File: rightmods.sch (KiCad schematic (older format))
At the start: 28 parts

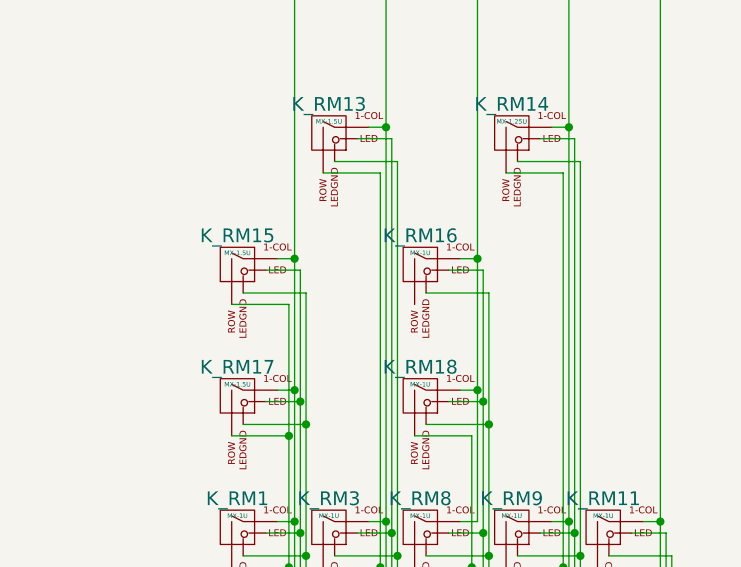
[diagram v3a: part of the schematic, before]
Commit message: Remove true HHKB row (LM8/9, SP15, RM15/16)
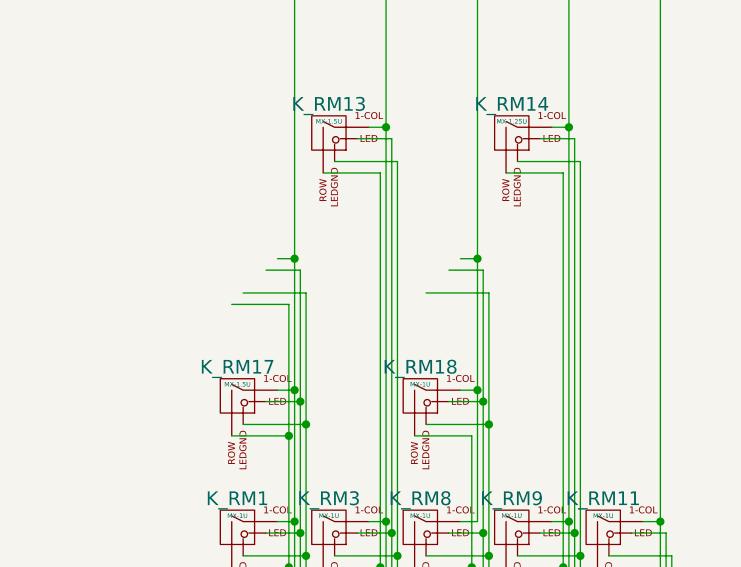
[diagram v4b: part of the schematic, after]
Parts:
- removed K_RM15: MX-1.5U, MX_Alps_Hybrid:MX-1.5U, symbol MX-1.5U
- removed K_RM16: MX-1U, MX_Alps_Hybrid:MX-1U, symbol MX-1U
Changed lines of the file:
@@
-$EndComp
-$Comp
-L MX-1.5U K_RM15
-U 1 1 59622322
-P 3775 2450
-F 0 "K_RM15" H 3775 2575 60  0000 C CNN
-F 1 "MX-1.5U" H 3775 2500 20  0000 C CNN
-F 2 "MX_Alps_Hybrid:MX-1.5U" H 3750 2425 60  0001 C CNN
-F 3 "" H 3750 2425 60  0001 C CNN
-	1    3775 2450
-	1    0    0    -1
 $EndComp
 $Comp
@@
 	1    0    0    -1
 $EndComp
-$Comp
-L MX-1U K_RM16
-U 1 1 59622BAC
-P 4575 2450
-F 0 "K_RM16" H 4575 2575 60  0000 C CNN
-F 1 "MX-1U" H 4575 2500 20  0000 C CNN
-F 2 "MX_Alps_Hybrid:MX-1U" H 4550 2425 60  0001 C CNN
-F 3 "" H 4550 2425 60  0001 C CNN
-	1    4575 2450
-	1    0    0    -1
-$EndComp

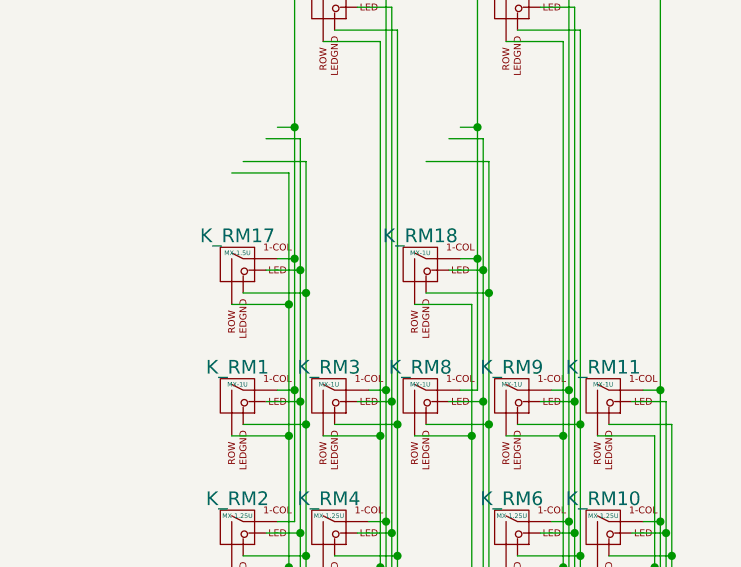
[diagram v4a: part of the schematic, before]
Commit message: Remove RM17, RM18
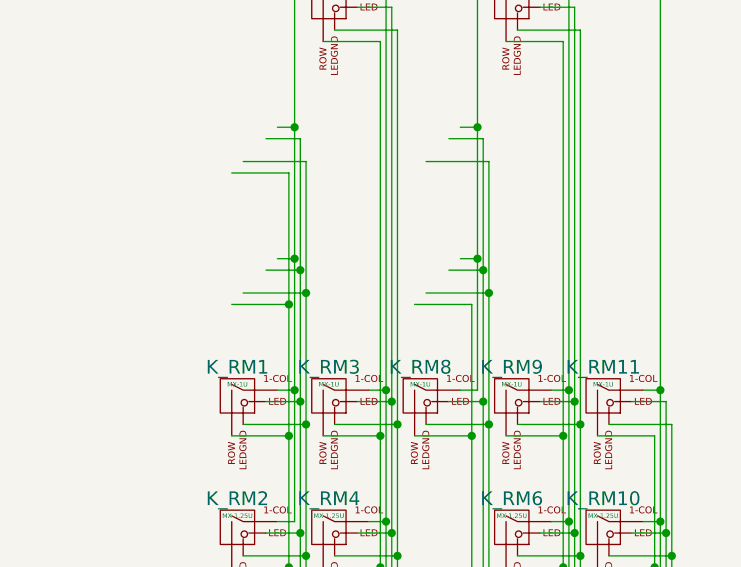
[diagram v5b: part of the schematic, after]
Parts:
- removed K_RM17: MX-1.5U, MX_Alps_Hybrid:MX-1.5U, symbol MX-1.5U
- removed K_RM18: MX-1U, MX_Alps_Hybrid:MX-1U, symbol MX-1U
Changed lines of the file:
@@
 rightmodscol1
-$Comp
-L MX-1.5U K_RM17
-U 1 1 59621BC9
-P 3775 3025
-F 0 "K_RM17" H 3775 3150 60  0000 C CNN
-F 1 "MX-1.5U" H 3775 3075 20  0000 C CNN
-F 2 "MX_Alps_Hybrid:MX-1.5U" H 3750 3000 60  0001 C CNN
-F 3 "" H 3750 3000 60  0001 C CNN
-	1    3775 3025
-	1    0    0    -1
-$EndComp
 $Comp
 L MX-1.5U K_RM13
@@
 	1    0    0    -1
 $EndComp
-$Comp
-L MX-1U K_RM18
-U 1 1 59622B20
-P 4575 3025
-F 0 "K_RM18" H 4575 3150 60  0000 C CNN
-F 1 "MX-1U" H 4575 3075 20  0000 C CNN
-F 2 "MX_Alps_Hybrid:MX-1U" H 4550 3000 60  0001 C CNN
-F 3 "" H 4550 3000 60  0001 C CNN
-	1    4575 3025
-	1    0    0    -1
-$EndComp

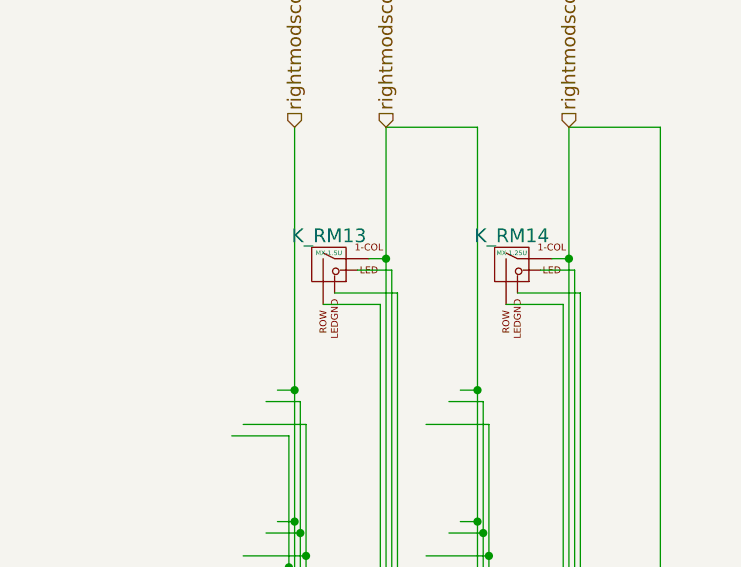
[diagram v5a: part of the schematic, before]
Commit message: Add in the Alps bottom row
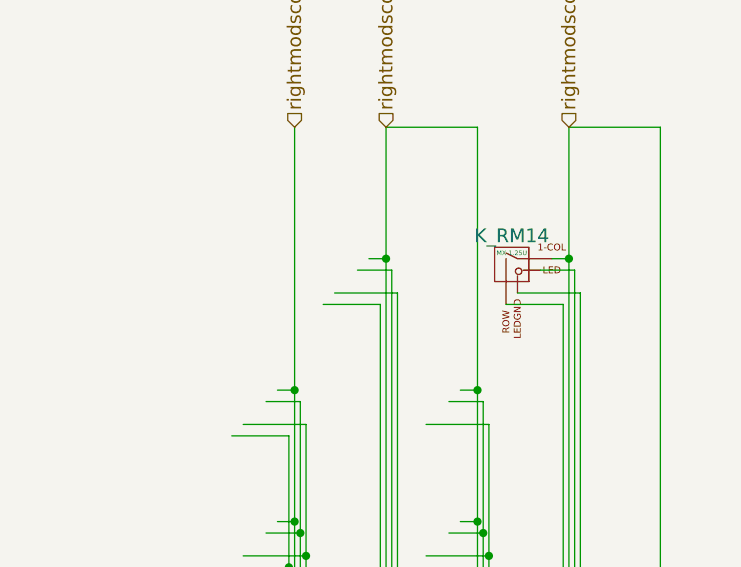
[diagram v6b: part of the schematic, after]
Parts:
- removed K_RM13: MX-1.5U, MX_Alps_Hybrid:MX-1.5U, symbol MX-1.5U
- K_RM14: footprint MX_Alps_Hybrid:MX-1.25U -> MX_Alps_Hybrid:ALPS-1.25U
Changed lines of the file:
@@
 rightmodscol1
-$Comp
-L MX-1.5U K_RM13
-U 1 1 596226D2
-P 4175 1875
-F 0 "K_RM13" H 4175 2000 60  0000 C CNN
-F 1 "MX-1.5U" H 4175 1925 20  0000 C CNN
-F 2 "MX_Alps_Hybrid:MX-1.5U" H 4150 1850 60  0001 C CNN
-F 3 "" H 4150 1850 60  0001 C CNN
-	1    4175 1875
-	1    0    0    -1
-$EndComp
 $Comp
 L MX-1.25U K_RM14
@@
 F 0 "K_RM14" H 4975 2000 60  0000 C CNN
 F 1 "MX-1.25U" H 4975 1925 20  0000 C CNN
-F 2 "MX_Alps_Hybrid:MX-1.25U" H 4950 1850 60  0001 C CNN
+F 2 "MX_Alps_Hybrid:ALPS-1.25U" H 4950 1850 60  0001 C CNN
 F 3 "" H 4950 1850 60  0001 C CNN
 	1    4975 1875

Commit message: Assign the footprints for every resistor and diode
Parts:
- DRM1, DRM2, DRM3, DRM4, DRM5: footprint (none) -> Diodes_SMD:D_SOD-323
- RRM1, RRM2, RRM3, RRM4, RRM5: footprint (none) -> Resistors_SMD:R_0603
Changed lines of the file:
@@
 F 0 "DRM1" H 4000 5550 50  0000 C CNN
 F 1 "1N4148WS" H 4000 5350 50  0000 C CNN
-F 2 "" H 4000 5450 50  0001 C CNN
+F 2 "Diodes_SMD:D_SOD-323" H 4000 5450 50  0001 C CNN
 F 3 "" H 4000 5450 50  0000 C CNN
 	1    4000 5450
@@
 F 0 "DRM2" H 4400 5550 50  0000 C CNN
 F 1 "1N4148WS" H 4400 5350 50  0000 C CNN
-F 2 "" H 4400 5450 50  0001 C CNN
+F 2 "Diodes_SMD:D_SOD-323" H 4400 5450 50  0001 C CNN
 F 3 "" H 4400 5450 50  0000 C CNN
 	1    4400 5450
@@
 F 0 "DRM3" H 4800 5550 50  0000 C CNN
 F 1 "1N4148WS" H 4800 5350 50  0000 C CNN
-F 2 "" H 4800 5450 50  0001 C CNN
+F 2 "Diodes_SMD:D_SOD-323" H 4800 5450 50  0001 C CNN
 F 3 "" H 4800 5450 50  0000 C CNN
 	1    4800 5450
@@
 F 0 "DRM4" H 5200 5550 50  0000 C CNN
 F 1 "1N4148WS" H 5200 5350 50  0000 C CNN
-F 2 "" H 5200 5450 50  0001 C CNN
+F 2 "Diodes_SMD:D_SOD-323" H 5200 5450 50  0001 C CNN
 F 3 "" H 5200 5450 50  0000 C CNN
 	1    5200 5450
@@
 F 0 "DRM5" H 5600 5550 50  0000 C CNN
 F 1 "1N4148WS" H 5600 5350 50  0000 C CNN
-F 2 "" H 5600 5450 50  0001 C CNN
+F 2 "Diodes_SMD:D_SOD-323" H 5600 5450 50  0001 C CNN
 F 3 "" H 5600 5450 50  0000 C CNN
 	1    5600 5450
@@
 F 0 "RRM1" V 4130 6500 50  0000 C CNN
 F 1 "2.2k" V 4050 6500 50  0000 C CNN
-F 2 "" V 3980 6500 50  0001 C CNN
+F 2 "Resistors_SMD:R_0603" V 3980 6500 50  0001 C CNN
 F 3 "" H 4050 6500 50  0000 C CNN
 	1    4050 6500
@@
 F 0 "RRM2" V 4530 6500 50  0000 C CNN
 F 1 "2.2k" V 4450 6500 50  0000 C CNN
-F 2 "" V 4380 6500 50  0001 C CNN
+F 2 "Resistors_SMD:R_0603" V 4380 6500 50  0001 C CNN
 F 3 "" H 4450 6500 50  0000 C CNN
 	1    4450 6500
@@
 F 0 "RRM3" V 4930 6500 50  0000 C CNN
 F 1 "2.2k" V 4850 6500 50  0000 C CNN
-F 2 "" V 4780 6500 50  0001 C CNN
+F 2 "Resistors_SMD:R_0603" V 4780 6500 50  0001 C CNN
 F 3 "" H 4850 6500 50  0000 C CNN
 	1    4850 6500
@@
 F 0 "RRM4" V 5330 6500 50  0000 C CNN
 F 1 "2.2k" V 5250 6500 50  0000 C CNN
-F 2 "" V 5180 6500 50  0001 C CNN
+F 2 "Resistors_SMD:R_0603" V 5180 6500 50  0001 C CNN
 F 3 "" H 5250 6500 50  0000 C CNN
 	1    5250 6500
@@
 F 0 "RRM5" V 5730 6500 50  0000 C CNN
 F 1 "2.2k" V 5650 6500 50  0000 C CNN
-F 2 "" V 5580 6500 50  0001 C CNN
+F 2 "Resistors_SMD:R_0603" V 5580 6500 50  0001 C CNN
 F 3 "" H 5650 6500 50  0000 C CNN
 	1    5650 6500

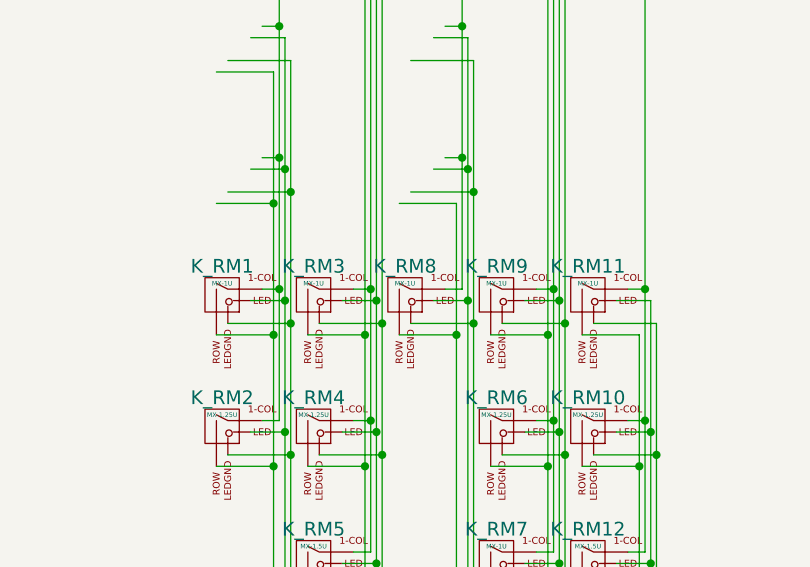
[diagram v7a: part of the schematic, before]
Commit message: Flipped schematic symbols for keys (except LS and bottom right mods)
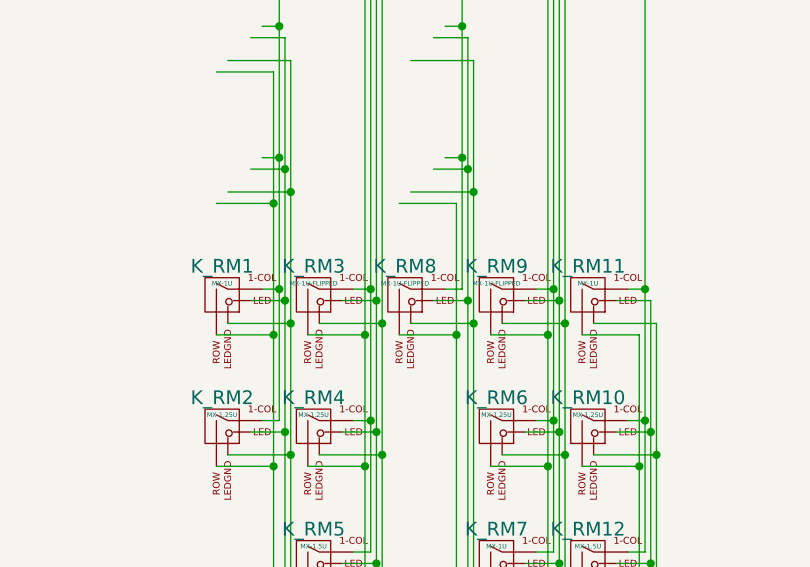
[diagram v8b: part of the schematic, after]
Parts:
- removed K_RM3, K_RM8, K_RM9: MX-1U, MX_Alps_Hybrid:MX-1U, symbol MX-1U
- added K_RM3, K_RM8, K_RM9: MX-1U-FLIPPED, symbol MX-1U-FLIPPED
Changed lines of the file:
@@
-$EndComp
-$Comp
-L MX-1U K_RM3
-U 1 1 5930D721
-P 4175 3600
-F 0 "K_RM3" H 4175 3725 60  0000 C CNN
-F 1 "MX-1U" H 4175 3650 20  0000 C CNN
-F 2 "MX_Alps_Hybrid:MX-1U" H 4150 3575 60  0001 C CNN
-F 3 "" H 4150 3575 60  0001 C CNN
-	1    4175 3600
-	1    0    0    -1
 $EndComp
 $Comp
@@
 F 3 "" H 4950 4725 60  0001 C CNN
 	1    4975 4750
-	1    0    0    -1
-$EndComp
-$Comp
-L MX-1U K_RM8
-U 1 1 5930DB99
-P 4575 3600
-F 0 "K_RM8" H 4575 3725 60  0000 C CNN
-F 1 "MX-1U" H 4575 3650 20  0000 C CNN
-F 2 "MX_Alps_Hybrid:MX-1U" H 4550 3575 60  0001 C CNN
-F 3 "" H 4550 3575 60  0001 C CNN
-	1    4575 3600
-	1    0    0    -1
-$EndComp
-$Comp
-L MX-1U K_RM9
-U 1 1 5930DBD5
-P 4975 3600
-F 0 "K_RM9" H 4975 3725 60  0000 C CNN
-F 1 "MX-1U" H 4975 3650 20  0000 C CNN
-F 2 "MX_Alps_Hybrid:MX-1U" H 4950 3575 60  0001 C CNN
-F 3 "" H 4950 3575 60  0001 C CNN
-	1    4975 3600
 	1    0    0    -1
 $EndComp
@@
 	5600 5800 5600 5600
 Connection ~ 4800 5800
+$Comp
+L MX-1U-FLIPPED K_RM3
+U 1 1 59905BE0
+P 4175 3600
+F 0 "K_RM3" H 4175 3725 60  0000 C CNN
+F 1 "MX-1U-FLIPPED" H 4175 3650 20  0000 C CNN
+F 2 "" H 4150 3575 60  0001 C CNN
+F 3 "" H 4150 3575 60  0001 C CNN
+	1    4175 3600
+	1    0    0    -1
+$EndComp
+$Comp
+L MX-1U-FLIPPED K_RM8
+U 1 1 59905CE0
+P 4575 3600
+F 0 "K_RM8" H 4575 3725 60  0000 C CNN
+F 1 "MX-1U-FLIPPED" H 4575 3650 20  0000 C CNN
+F 2 "" H 4550 3575 60  0001 C CNN
+F 3 "" H 4550 3575 60  0001 C CNN
+	1    4575 3600
+	1    0    0    -1
+$EndComp
+$Comp
+L MX-1U-FLIPPED K_RM9
+U 1 1 59905DDE
+P 4975 3600
+F 0 "K_RM9" H 4975 3725 60  0000 C CNN
+F 1 "MX-1U-FLIPPED" H 4975 3650 20  0000 C CNN
+F 2 "" H 4950 3575 60  0001 C CNN
+F 3 "" H 4950 3575 60  0001 C CNN
+	1    4975 3600
+	1    0    0    -1
+$EndComp
 $EndSCHEMATC
